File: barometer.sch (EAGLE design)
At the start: 83 parts, among them IC1 MIC5225-3.3v, IC2 TPS5410, IC3 ZPA2326-0311A-R, U1 MCP4725, U2 LTC2850, U3 PCA9306, U4 MAX3221, U5 XC6215XC6215B182NR, U6 Tiny85-20-SMT, X2 1751264, X3 1751248

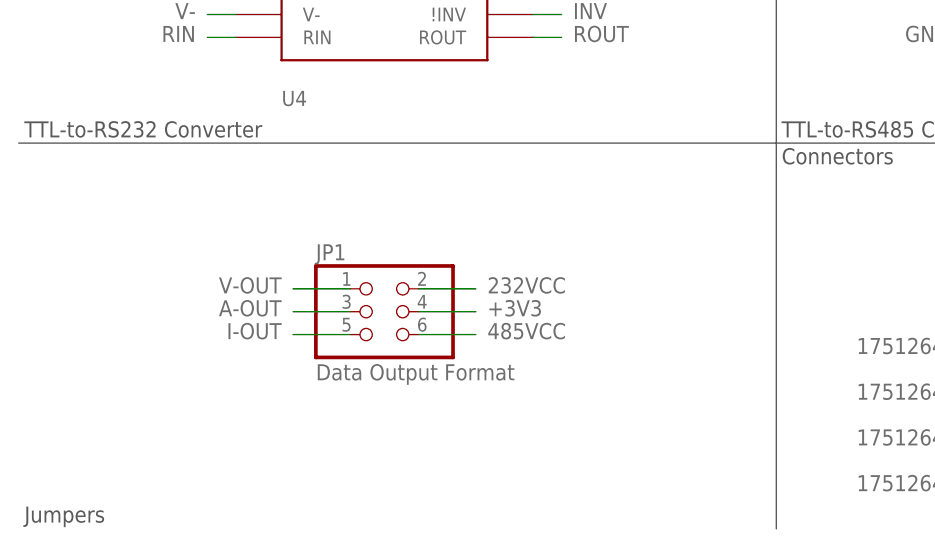
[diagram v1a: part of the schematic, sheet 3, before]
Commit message: Replace surface-mount jumper with through-hole SPDT sliding switch
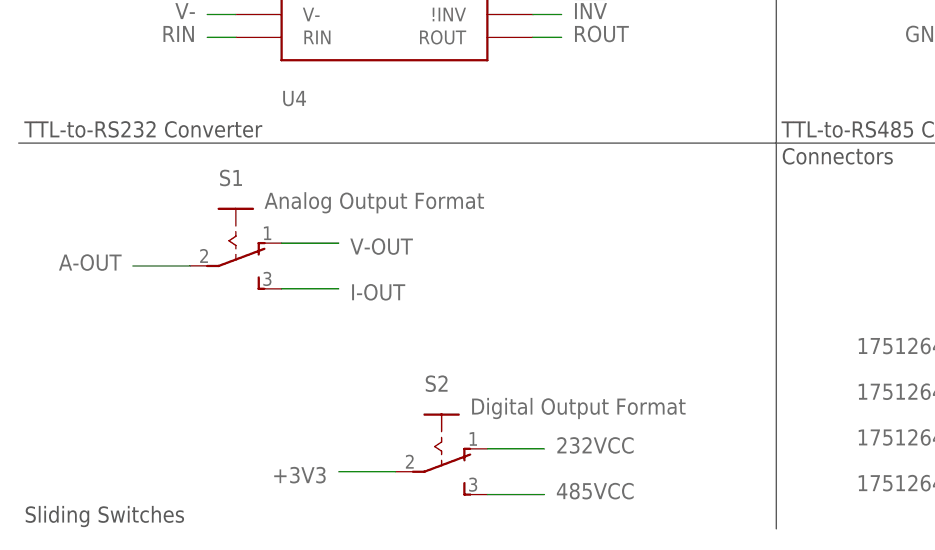
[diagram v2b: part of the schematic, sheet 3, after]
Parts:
- removed JP1: Data Output Format, pinhead-2:PINHD-2X03_2.54-SMD-90°
- added S1: Analog Output Format, switch:255SB
- added S2: Digital Output Format, switch:255SB
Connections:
- net +3V3: now also S2.P; no longer JP1.4
- net 232VCC: now also S2.O; no longer JP1.2
- net 485VCC: now also S2.S; no longer JP1.6
- net A-OUT: now also S1.P; no longer JP1.3
- net I-OUT: now also S1.S; no longer JP1.5
- net V-OUT: now also S1.O; no longer JP1.1
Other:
- note added: "Sliding Switches"
- note removed: "Jumpers"
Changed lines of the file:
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@@
 <part name="TP0" library="testpad" deviceset="PTR1" device="B1,27"/>
 <part name="FRAME2" library="microbuilder" deviceset="FRAME_A4" device=""/>
-<part name="JP1" library="pinhead-2" deviceset="PINHD-2X03" device="_2.54-SMD-90°" value="Data Output Format"/>
 <part name="FRAME6" library="microbuilder" deviceset="FRAME_A4" device=""/>
 <part name="FRAME5" library="microbuilder" deviceset="FRAME_A4" device=""/>
@@
 <part name="X3" library="con-phoenix-350" deviceset="1751248" device=""/>
 <part name="X2" library="con-phoenix-350" deviceset="1751264" device=""/>
+<part name="S1" library="switch" deviceset="255SB" device="" value="Analog Output Format"/>
+<part name="S2" library="switch" deviceset="255SB" device="" value="Digital Output Format"/>
 </parts>
 <sheets>
@@
 <text x="4.445" y="90.17" size="1.778" layer="97" font="vector">TTL-to-RS232 Peripherals</text>
 <text x="172.72" y="20.32" size="2.54" layer="97" font="vector">Data Output Interface</text>
-<text x="4.445" y="4.5085" size="1.778" layer="97" font="vector">Jumpers</text>
+<text x="4.445" y="4.5085" size="1.778" layer="97" font="vector">Sliding Switches</text>
 <text x="4.445" y="133.096" size="1.778" layer="97" font="vector">Test Points</text>
 <text x="88.5825" y="46.101" size="1.778" layer="97" font="vector" rot="MR0" align="top-right">Connectors</text>
@@
 <attribute name="VALUE" x="124.1044" y="49.53" size="2.0828" layer="96" ratio="10" rot="SR0"/>
 </instance>
-<instance part="JP1" gate="A" x="43.18" y="27.94"/>
 <instance part="C3" gate="G$1" x="22.86" y="111.76"/>
 <instance part="C4" gate="G$1" x="33.02" y="111.76"/>
@@
 <instance part="X2" gate="-3" x="120.65" y="13.97" rot="R180"/>
 <instance part="X2" gate="-4" x="120.65" y="8.89" rot="R180"/>
+<instance part="S1" gate="1" x="27.94" y="35.56" rot="R270"/>
+<instance part="S2" gate="1" x="50.8" y="12.7" rot="R270"/>
 </instances>
 <busses>
@@
 <net name="+3V3" class="0">
 <segment>
-<wire x1="48.26" y1="27.94" x2="54.61" y2="27.94" width="0.1524" layer="91"/>
-<label x="55.88" y="29.21" size="1.778" layer="95" font="vector" rot="MR180"/>
-<pinref part="JP1" gate="A" pin="4"/>
+<wire x1="39.37" y1="10.16" x2="45.72" y2="10.16" width="0.1524" layer="91"/>
+<label x="38.1" y="8.89" size="1.778" layer="95" font="vector" rot="MR0"/>
+<pinref part="S2" gate="1" pin="P"/>
 </segment>
 <segment>
@@
 </segment>
 <segment>
-<wire x1="48.26" y1="30.48" x2="54.61" y2="30.48" width="0.1524" layer="91"/>
-<label x="55.88" y="31.75" size="1.778" layer="95" font="vector" rot="MR180"/>
-<pinref part="JP1" gate="A" pin="2"/>
+<wire x1="55.88" y1="12.7" x2="62.23" y2="12.7" width="0.1524" layer="91"/>
+<label x="63.5" y="13.97" size="1.778" layer="95" font="vector" rot="MR180"/>
+<pinref part="S2" gate="1" pin="O"/>
 </segment>
 </net>
@@
 </segment>
 <segment>
-<wire x1="48.26" y1="25.4" x2="54.61" y2="25.4" width="0.1524" layer="91"/>
-<label x="55.88" y="26.67" size="1.778" layer="95" font="vector" rot="MR180"/>
-<pinref part="JP1" gate="A" pin="6"/>
+<wire x1="55.88" y1="7.62" x2="62.23" y2="7.62" width="0.1524" layer="91"/>
+<label x="63.5" y="8.89" size="1.778" layer="95" font="vector" rot="MR180"/>
+<pinref part="S2" gate="1" pin="S"/>
 </segment>
 </net>
@@
 </segment>
 <segment>
-<wire x1="40.64" y1="27.94" x2="34.29" y2="27.94" width="0.1524" layer="91"/>
-<label x="33.02" y="29.21" size="1.778" layer="95" font="vector" rot="R180"/>
-<pinref part="JP1" gate="A" pin="3"/>
+<wire x1="22.86" y1="33.02" x2="16.51" y2="33.02" width="0.1524" layer="91"/>
+<label x="15.24" y="34.29" size="1.778" layer="95" font="vector" rot="R180"/>
+<pinref part="S1" gate="1" pin="P"/>
 </segment>
 </net>
@@
 </segment>
 <segment>
-<wire x1="40.64" y1="30.48" x2="34.29" y2="30.48" width="0.1524" layer="91"/>
-<label x="33.02" y="31.75" size="1.778" layer="95" font="vector" rot="R180"/>
-<pinref part="JP1" gate="A" pin="1"/>
+<wire x1="39.37" y1="35.56" x2="33.02" y2="35.56" width="0.1524" layer="91"/>
+<label x="40.64" y="34.29" size="1.778" layer="95" font="vector"/>
+<pinref part="S1" gate="1" pin="O"/>
 </segment>
 </net>
 <net name="I-OUT" class="0">
 <segment>
-<wire x1="40.64" y1="25.4" x2="34.29" y2="25.4" width="0.1524" layer="91"/>
-<label x="33.02" y="26.67" size="1.778" layer="95" font="vector" rot="R180"/>
-<pinref part="JP1" gate="A" pin="5"/>
-</segment>
-</net>
+<wire x1="39.37" y1="30.48" x2="33.02" y2="30.48" width="0.1524" layer="91"/>
+<label x="40.64" y="29.21" size="1.778" layer="95" font="vector"/>
+<pinref part="S1" gate="1" pin="S"/>
+</segment>
+</net>

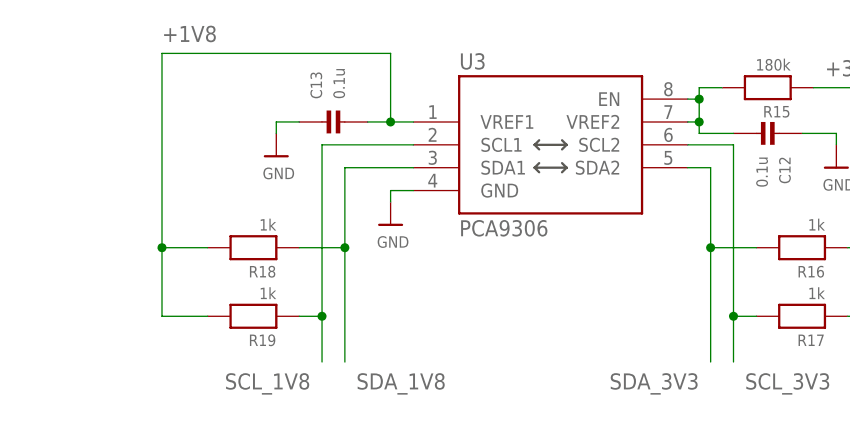
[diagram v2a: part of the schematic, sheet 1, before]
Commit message: Fix incorrect connections from/to MAX3221 and PCA9306
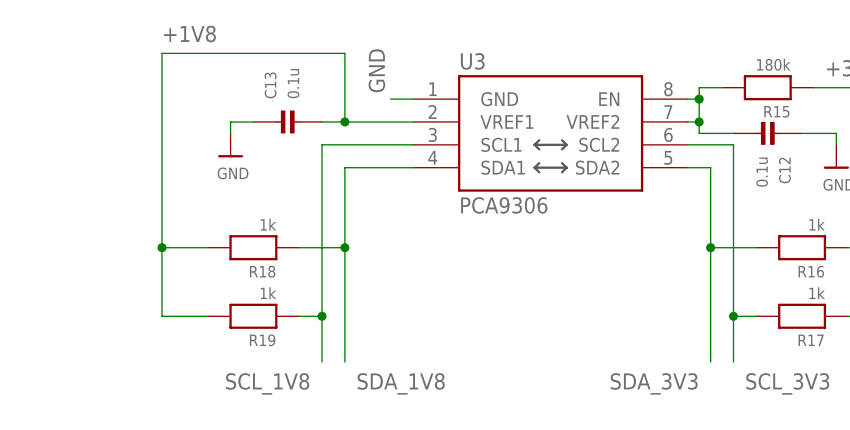
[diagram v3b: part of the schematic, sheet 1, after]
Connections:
- net DIN: no longer SJ2.2
- net DOUT: now also SJ4.2
- net RIN: now also SJ2.2
- net ROUT: no longer SJ4.2
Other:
- moved on the sheet: C13, U3

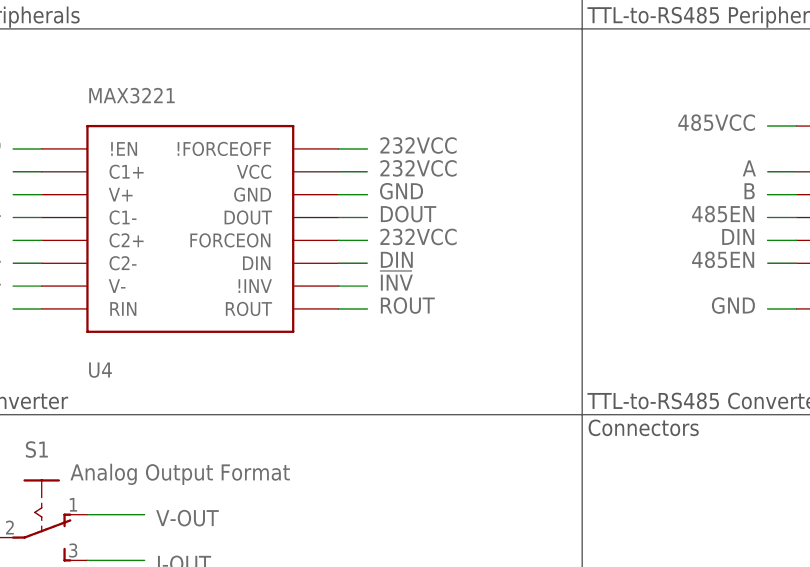
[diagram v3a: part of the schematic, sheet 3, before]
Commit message: Remove unused signal and net
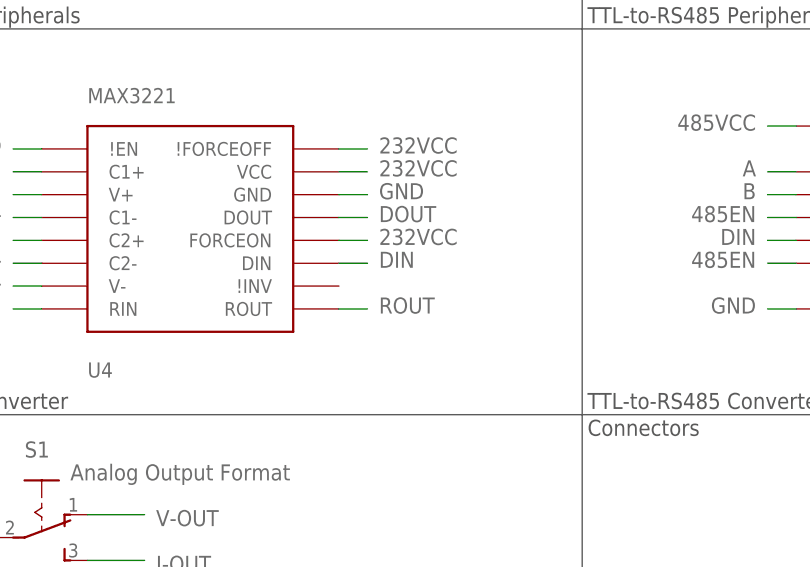
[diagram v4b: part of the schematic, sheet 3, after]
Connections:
- removed net !INV: U4.\!INV
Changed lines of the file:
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@@
-</segment>
-</net>
-<net name="!INV" class="0">
-<segment>
-<pinref part="U4" gate="G$1" pin="\!INV"/>
-<wire x1="60.96" y1="60.96" x2="64.135" y2="60.96" width="0.1524" layer="91"/>
-<label x="65.405" y="62.23" size="1.778" layer="95" font="vector" rot="MR180"/>
 </segment>
 </net>

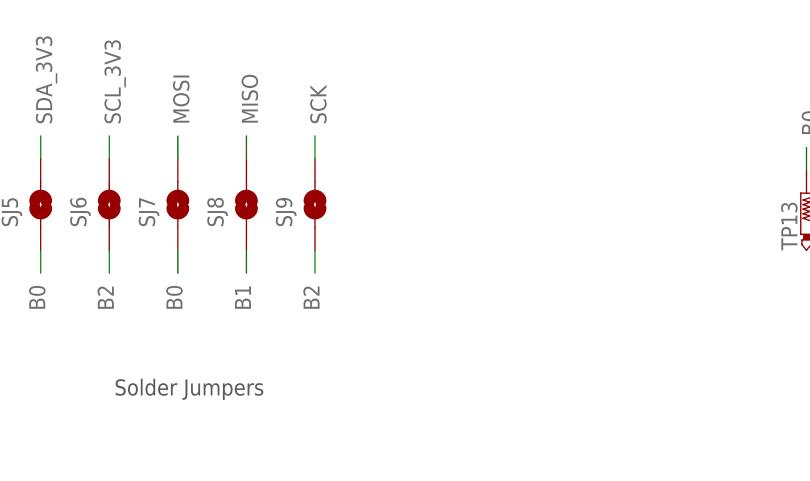
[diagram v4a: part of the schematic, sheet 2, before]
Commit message: Connect microcontroller to RS-232 and RS-485 transceivers
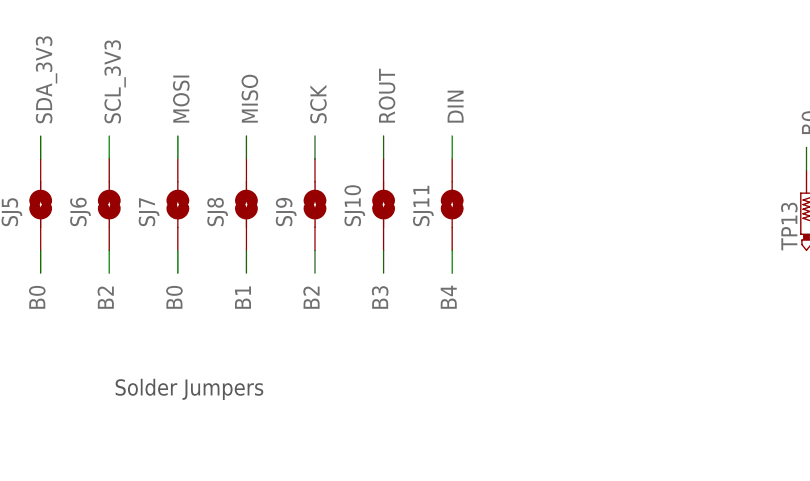
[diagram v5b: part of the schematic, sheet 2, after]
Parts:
- added SJ10, SJ11: SOLDERJUMPERTRACE, SparkFun-Retired:SOLDERJUMPERTRACE
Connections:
- net B3: now also SJ10.1
- net B4: now also SJ11.1
- net DIN: now also SJ11.2
- net ROUT: now also SJ10.2
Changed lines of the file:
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@@
 <setting verticaltext="up"/>
 </settings>
-<grid distance="0.025" unitdist="inch" unit="inch" style="lines" multiple="1" display="no" altdistance="0.01" altunitdist="inch" altunit="inch"/>
+<grid distance="0.05" unitdist="inch" unit="inch" style="lines" multiple="1" display="yes" altdistance="0.01" altunitdist="inch" altunit="inch"/>
 <layers>
 <layer number="1" name="Top" color="4" fill="1" visible="no" active="no"/>
@@
 <part name="S2" library="switch" deviceset="255SB" device="" value="Digital Output Format"/>
 <part name="U3" library="SparkFun-IC-Comms" deviceset="PCA9306" device="" value="PCA9306"/>
+<part name="SJ10" library="SparkFun-Retired" deviceset="SOLDERJUMPER" device="TRACE"/>
+<part name="SJ11" library="SparkFun-Retired" deviceset="SOLDERJUMPER" device="TRACE"/>
 </parts>
 <sheets>
@@
 </instance>
 <instance part="JP2" gate="G$1" x="48.26" y="45.72"/>
+<instance part="SJ10" gate="1" x="72.39" y="134.62" smashed="yes" rot="R90">
+<attribute name="NAME" x="69.85" y="132.08" size="1.778" layer="95" rot="R90"/>
+</instance>
+<instance part="SJ11" gate="1" x="80.01" y="134.62" smashed="yes" rot="R90">
+<attribute name="NAME" x="77.47" y="132.08" size="1.778" layer="95" rot="R90"/>
+</instance>
 </instances>
 <busses>
@@
 <label x="135.89" y="142.24" size="1.778" layer="95" rot="R90"/>
 </segment>
+<segment>
+<pinref part="SJ10" gate="1" pin="1"/>
+<wire x1="72.39" y1="129.54" x2="72.39" y2="127" width="0.1524" layer="91"/>
+<label x="71.12" y="125.73" size="1.778" layer="95" rot="R270"/>
+</segment>
 </net>
 <net name="B4" class="0">
@@
 <label x="130.81" y="142.24" size="1.778" layer="95" rot="R90"/>
 </segment>
+<segment>
+<pinref part="SJ11" gate="1" pin="1"/>
+<wire x1="80.01" y1="129.54" x2="80.01" y2="127" width="0.1524" layer="91"/>
+<label x="78.74" y="125.73" size="1.778" layer="95" rot="R270"/>
+</segment>
 </net>
 <net name="B0" class="0">
@@
 </segment>
 </net>
+<net name="ROUT" class="0">
+<segment>
+<pinref part="SJ10" gate="1" pin="2"/>
+<wire x1="72.39" y1="139.7" x2="72.39" y2="142.24" width="0.1524" layer="91"/>
+<label x="73.66" y="143.51" size="1.778" layer="95" rot="R90"/>
+</segment>
+</net>
+<net name="DIN" class="0">
+<segment>
+<pinref part="SJ11" gate="1" pin="2"/>
+<wire x1="80.01" y1="139.7" x2="80.01" y2="142.24" width="0.1524" layer="91"/>
+<label x="81.28" y="143.51" size="1.778" layer="95" rot="R90"/>
+</segment>
+</net>

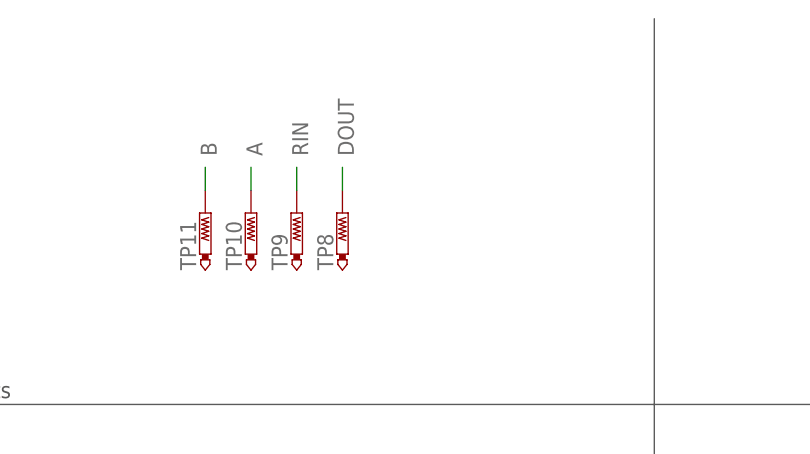
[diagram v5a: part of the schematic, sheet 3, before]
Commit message: Connect analog output pins to test points
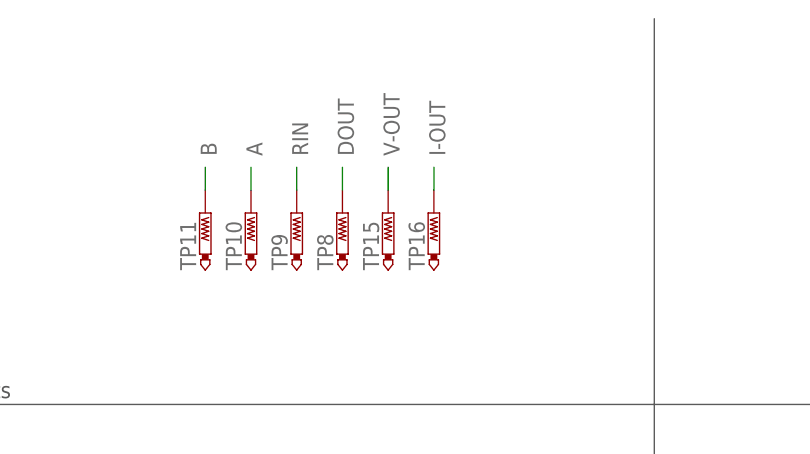
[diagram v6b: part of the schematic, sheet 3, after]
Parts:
- added TP15, TP16: PTR1B1,27, testpad:PTR1B1,27
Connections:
- net I-OUT: now also TP16.TP
- net V-OUT: now also TP15.TP
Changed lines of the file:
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@@
 <part name="SJ10" library="SparkFun-Retired" deviceset="SOLDERJUMPER" device="TRACE"/>
 <part name="SJ11" library="SparkFun-Retired" deviceset="SOLDERJUMPER" device="TRACE"/>
+<part name="TP15" library="testpad" deviceset="PTR1" device="B1,27"/>
+<part name="TP16" library="testpad" deviceset="PTR1" device="B1,27"/>
 </parts>
 <sheets>
@@
 <instance part="S1" gate="1" x="27.94" y="35.56" rot="R270"/>
 <instance part="S2" gate="1" x="50.8" y="12.7" rot="R270"/>
+<instance part="TP15" gate="G$1" x="58.42" y="153.67"/>
+<instance part="TP16" gate="G$1" x="63.5" y="153.67"/>
 </instances>
 <busses>
@@
 <pinref part="S1" gate="1" pin="O"/>
 </segment>
+<segment>
+<pinref part="TP15" gate="G$1" pin="TP"/>
+<wire x1="58.42" y1="156.21" x2="58.42" y2="158.75" width="0.1524" layer="91"/>
+<label x="59.69" y="160.02" size="1.778" layer="95" rot="R90"/>
+</segment>
 </net>
 <net name="I-OUT" class="0">
@@
 <pinref part="S1" gate="1" pin="S"/>
 </segment>
-</net>
+<segment>
+<pinref part="TP16" gate="G$1" pin="TP"/>
+<wire x1="63.5" y1="156.21" x2="63.5" y2="158.75" width="0.1524" layer="91"/>
+<label x="64.77" y="160.02" size="1.778" layer="95" rot="R90"/>
+</segment>
+</net>

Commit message: Rename self-created libraries
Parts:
- IC3: device MurataZPA:ZPA2326-0311A-R -> barometer-murata:ZPA2326-0311A-R
- U5: device XC6215:XC6215XC6215B182NR -> v-regulator-torex:XC6215XC6215B182NR
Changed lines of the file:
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@@
 <part name="C1" library="microbuilder" deviceset="CAP_CERAMIC" device="0603" value="10u"/>
 <part name="C2" library="microbuilder" deviceset="CAP_CERAMIC" device="0603" value="10u"/>
-<part name="U5" library="XC6215" deviceset="XC6215" device="XC6215B182NR"/>
+<part name="U5" library="v-regulator-torex" deviceset="XC6215" device="XC6215B182NR"/>
 <part name="C10" library="microbuilder" deviceset="CAP_CERAMIC" device="0603" value="1u"/>
 <part name="C11" library="microbuilder" deviceset="CAP_CERAMIC" device="0603" value="1u"/>
@@
 <part name="R21" library="microbuilder" deviceset="RESISTOR" device="0603" value="3.24k"/>
 <part name="R22" library="microbuilder" deviceset="RESISTOR" device="0603" value="1.78k"/>
-<part name="IC3" library="MurataZPA" deviceset="ZPA2326" device="-0311A-R"/>
+<part name="IC3" library="barometer-murata" deviceset="ZPA2326" device="-0311A-R"/>
 <part name="R23" library="microbuilder" deviceset="RESISTOR" device="0603" value="1k"/>
 <part name="C19" library="microbuilder" deviceset="CAP_CERAMIC" device="0603" value="0.1u"/>
